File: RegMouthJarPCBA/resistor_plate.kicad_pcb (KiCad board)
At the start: 2 copper layers, 48.3 x 48.3 mm, 9 parts, among them P1 CONN_4

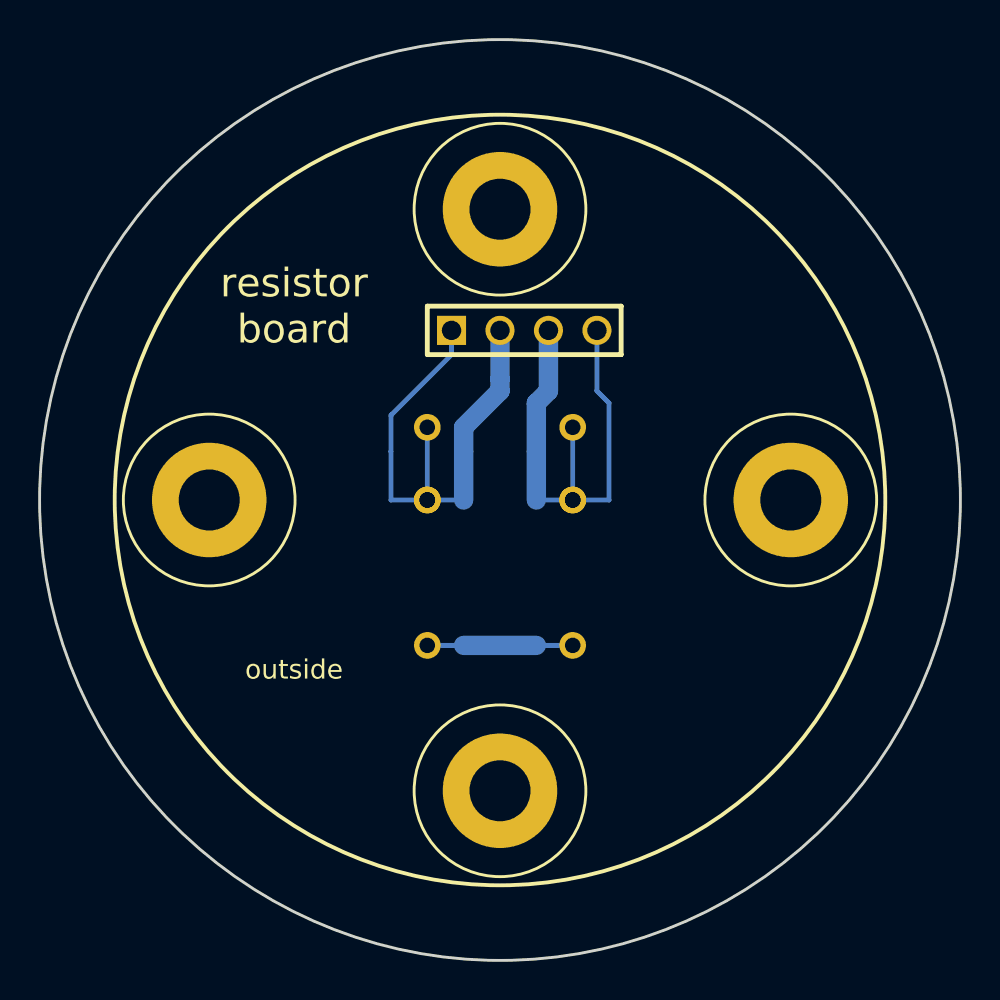
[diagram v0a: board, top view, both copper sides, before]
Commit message: updating resistor board to v2.
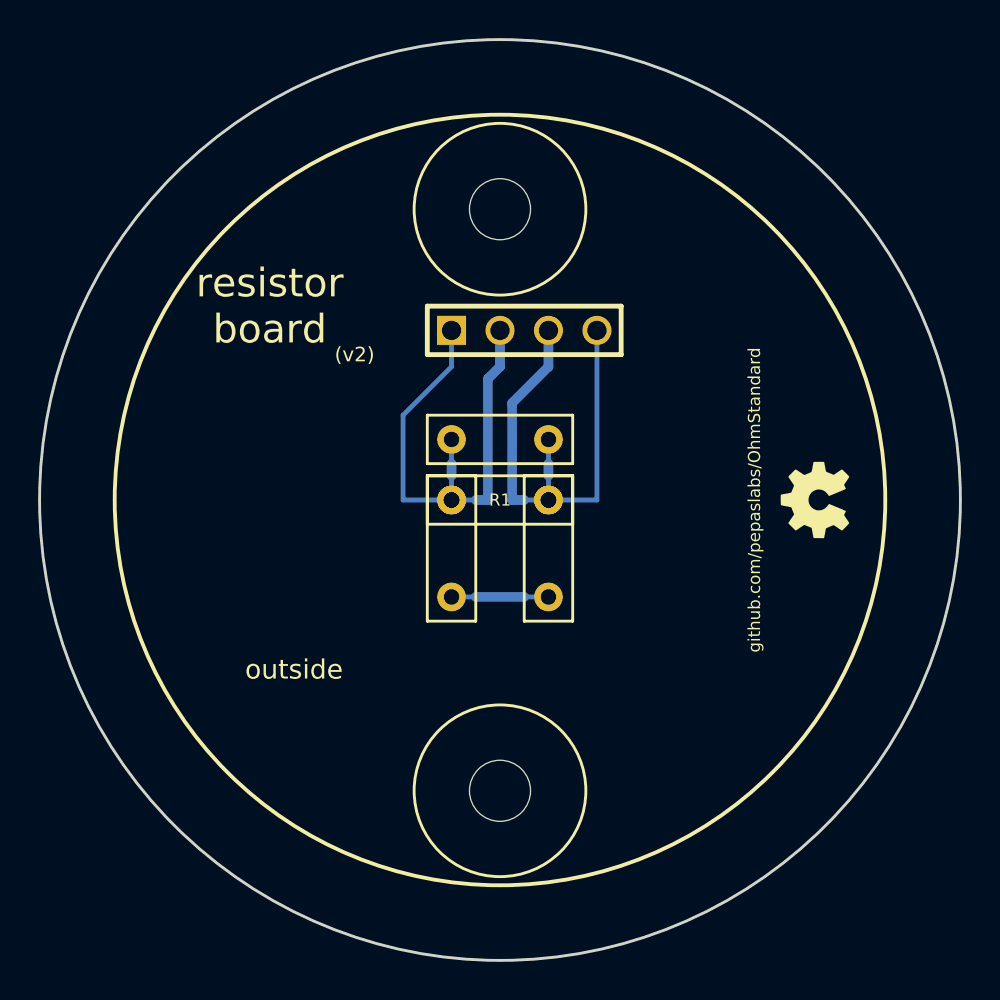
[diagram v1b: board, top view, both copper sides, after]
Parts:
- removed H*** (x2): Val**, hole_M3
- removed R3 (x3): Val*, R3
- added G***: OSHW-logo_silkscreen-front_4mm, OSHW-logo_silkscreen-front_4mm, F.Cu at (232.4, 138.4)
- added R***: VAL**, R_BOX_02, F.Cu at (213.4, 135.3)
- added R***: VAL**, R_BOX_02, F.Cu at (213.4, 138.4)
- added R***: VAL**, R_BOX_02, F.Cu at (218.4, 138.4)
- H1, H2: footprint hole_M3 -> hole_M3_NPTH
- R1: footprint R3 -> R_BOX_02; moved to F.Cu
- moved R1 2.54 mm to (213.4, 138.4)
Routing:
- net (no net): track 15.2 -> 5.08 mm
- net N-000004: track 22.1 -> 26.2 mm
- net N-000003: track 23.7 -> 26.7 mm
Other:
- board text added: "(v2)"
- board text added: "github.com/pepaslabs/OhmStandard"
- board text added: "parallel resistors"
- board text added: "series resistors"
- board text added: "single resistor"

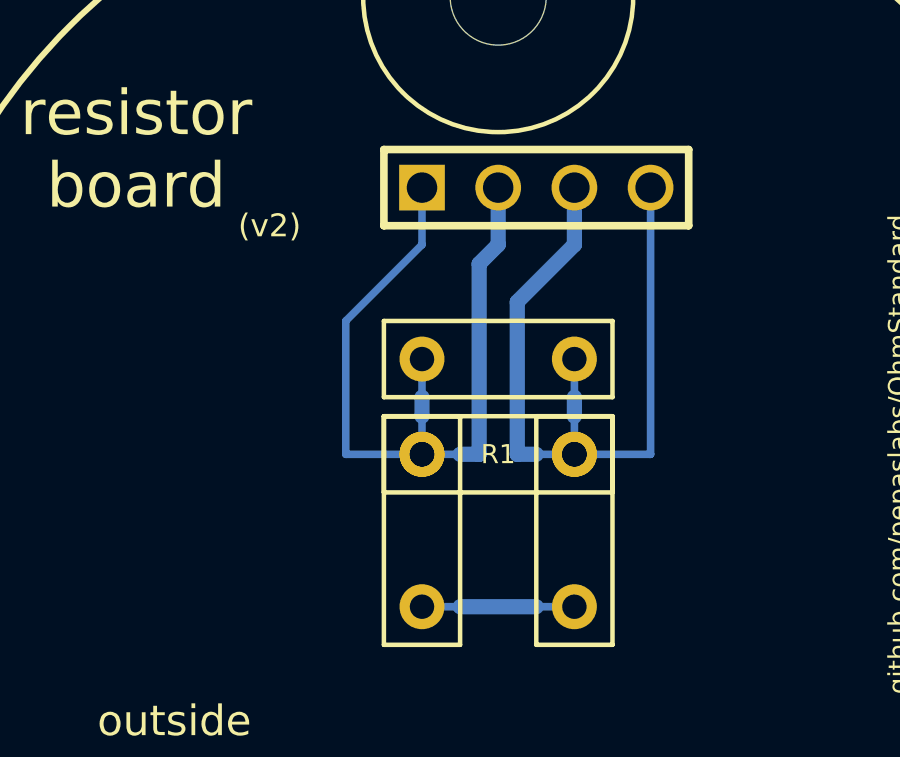
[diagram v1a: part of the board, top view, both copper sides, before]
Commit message: updating resistor board to v3.
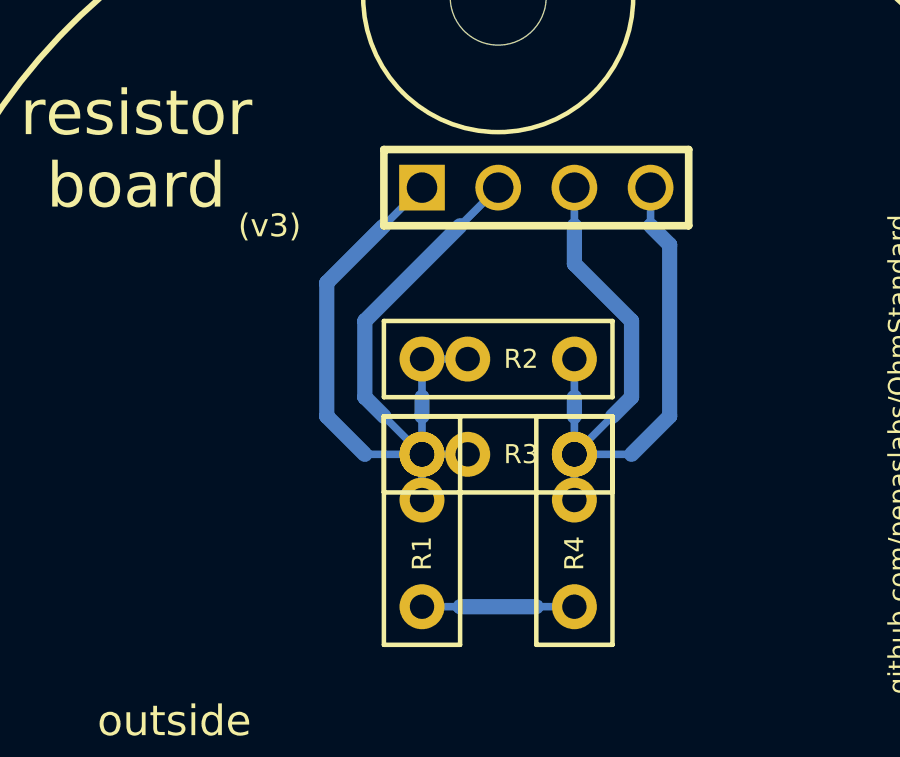
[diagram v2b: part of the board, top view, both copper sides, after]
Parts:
- removed R*** (x3): VAL**, R_BOX_02
- added R2: R, R_BOX, F.Cu at (213.4, 135.3)
- added R3: R, R_BOX, F.Cu at (213.4, 138.4)
- added R4: R, R_BOX, F.Cu at (218.4, 138.4)
- R1: footprint R_BOX_02 -> R_BOX
- turned R1 to 270 degrees
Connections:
- P1 pad 3: N-000004 -> N-000002
- P1 pad 4: N-000004 -> N-000002
- R1 pad 1: N-000003 -> N-000001
- R1 pad 2: N-000004 -> N-000003
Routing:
- net N-000002: track 0.00 -> 28.0 mm
- net N-000004: track 26.2 -> 0.00 mm
- net N-000003: track 26.7 -> 34.6 mm
- net (no net): track 5.08 -> 0.00 mm
- net N-000001: track 0.00 -> 1.52 mm
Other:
- board text added: "(v3)"
- board text removed: "(v2)"
